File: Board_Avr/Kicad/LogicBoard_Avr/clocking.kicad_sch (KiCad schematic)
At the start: 5 parts, among them X1 ASV-12.000MHZ-EJ-T, Y1 ABLS-20.000MHz-16-A-4-H-T

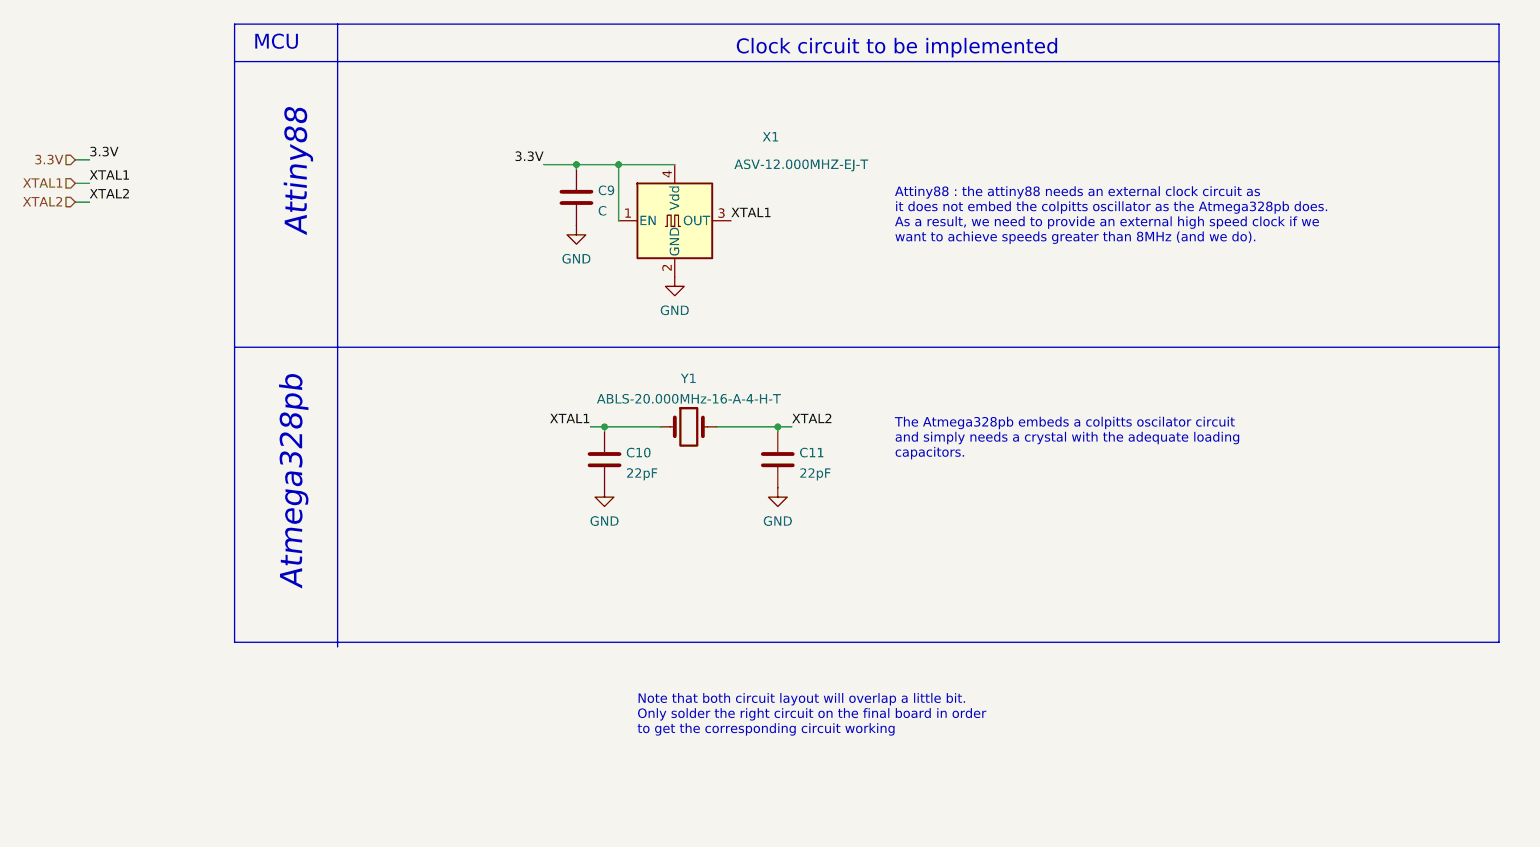
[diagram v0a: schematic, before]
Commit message: Added several external connections and reworked leds and output signals
Signed-off-by: bebenlebricolo <benoittarrade@hotmail.fr>
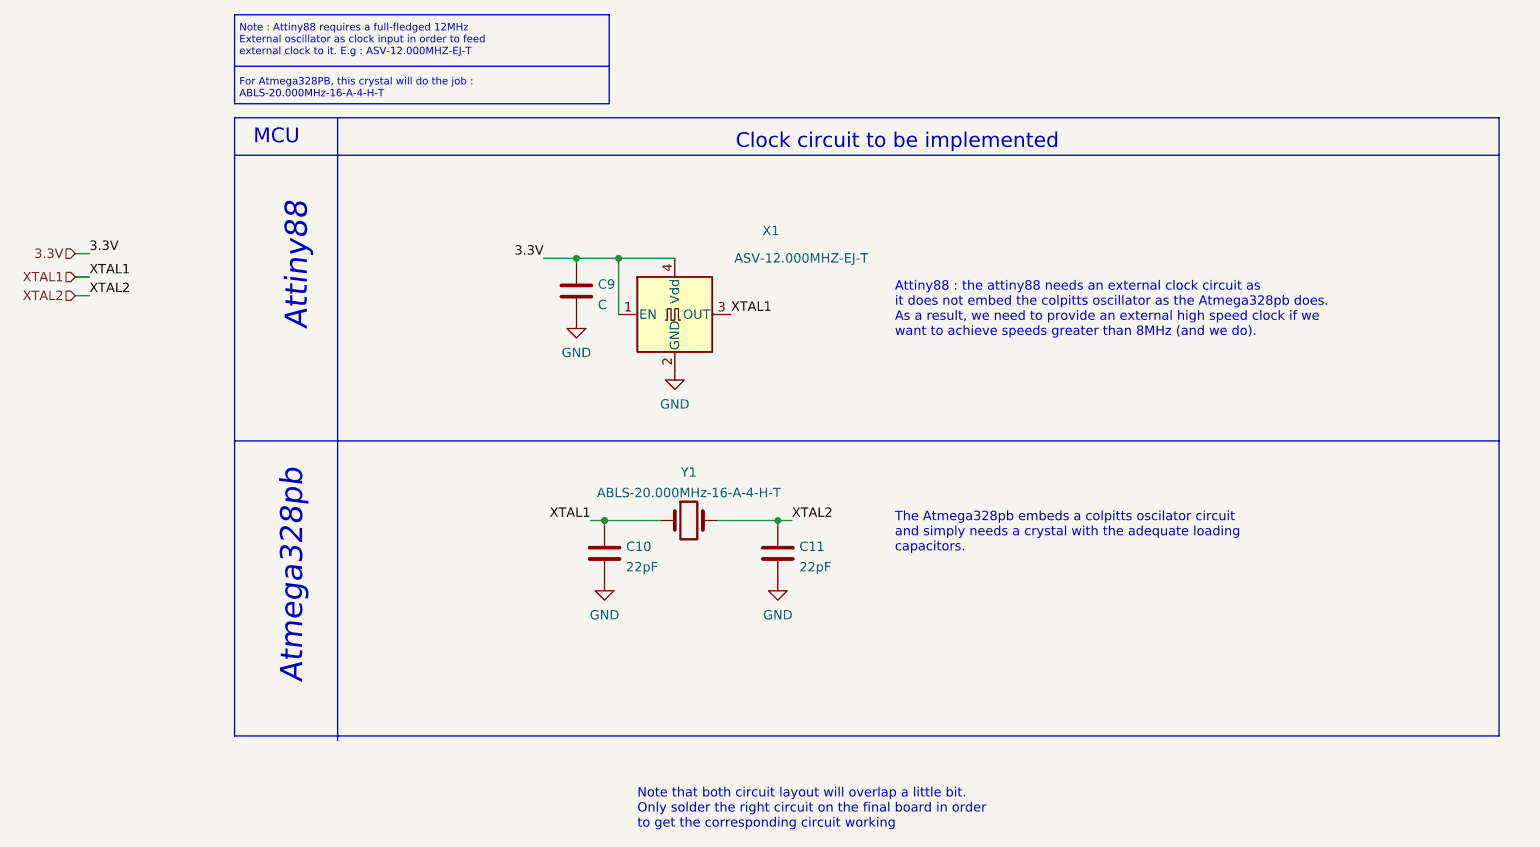
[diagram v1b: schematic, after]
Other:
- note added: "For Atmega328PB, this crystal will do the job : ABLS-20.000MHz-16-A-4-H-T"
- note added: "Note : Attiny88 requires a full-fledged 12MHz External oscillator as clock input in order to feed external clock to it. E.g : ASV-12.000MHZ-EJ-T"
- moved on the sheet: C10, C11, C9, X1, Y1

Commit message: Started routing all traces
Signed-off-by: bebenlebricolo <benoittarrade@hotmail.fr>
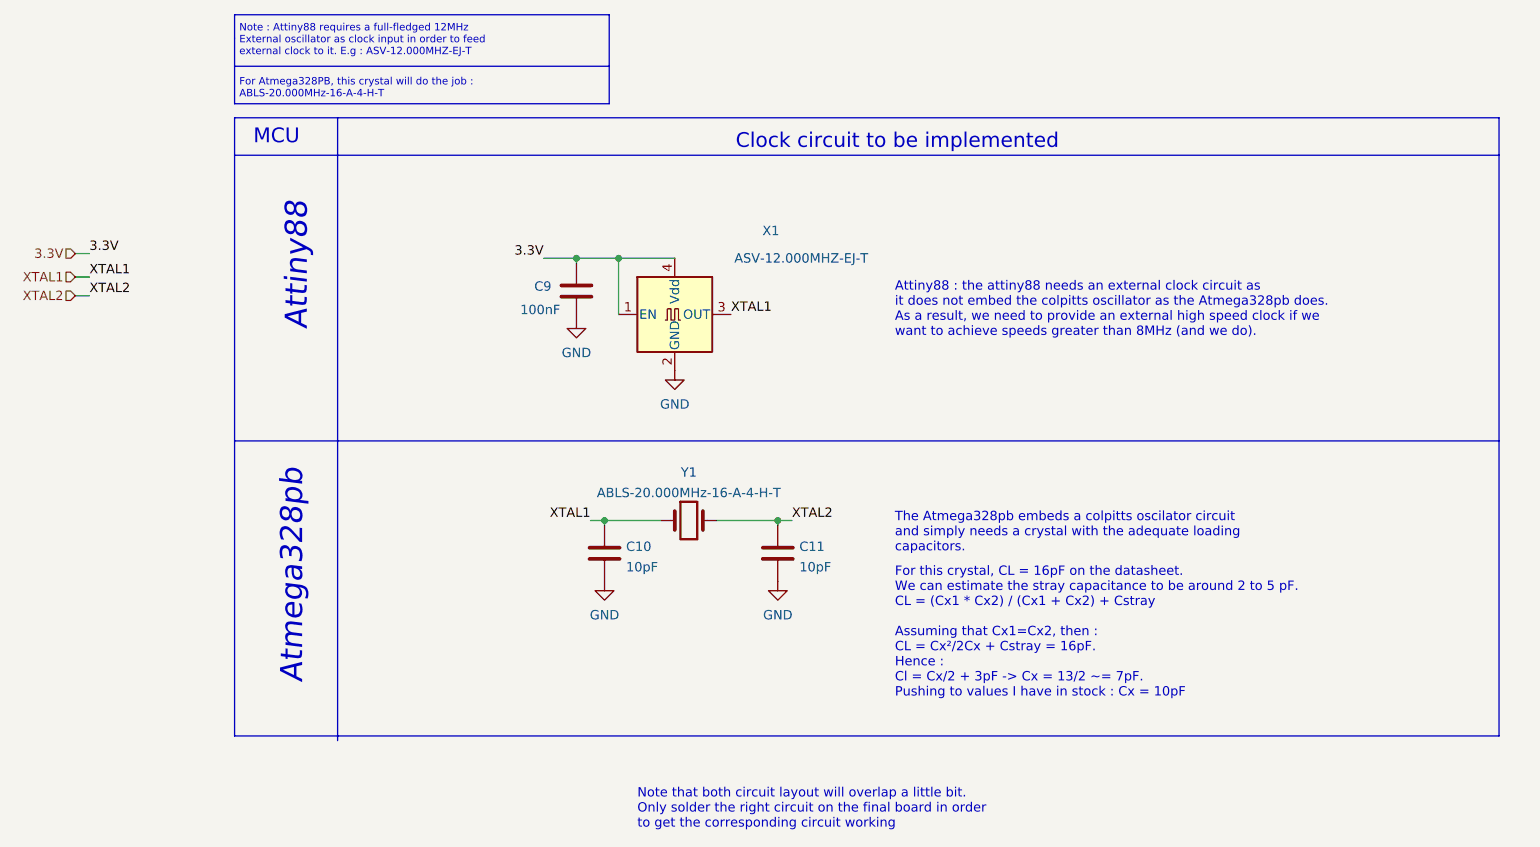
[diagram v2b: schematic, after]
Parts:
- C10, C11: value 22pF -> 10pF; footprint (none) -> Capacitor_SMD:C_1206_3216Metric
- C9: value C -> 100nF; footprint (none) -> Capacitor_SMD:C_1206_3216Metric
- Y1: footprint (none) -> Crystal:Crystal_SMD_HC49-SD
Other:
- note added: "For this crystal, CL = 16pF on the datasheet. We can estimate the stray capacitance to be around 2 to 5 pF. CL = (Cx1 * Cx2) / (Cx1 + Cx2) + Cstray Assuming that Cx1=Cx2, then : CL = Cx²/2Cx + Cstray = 16pF. Hence : Cl = Cx/2 + 3pF -> Cx = 13/2 ~= 7pF. Pushing to values I have in stock : Cx = 10pF"
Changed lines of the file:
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@@
+    (effects (font (size 1.27 1.27)) (justify left bottom))
+  )
+  (text "For this crystal, CL = 16pF on the datasheet.\nWe can estimate the stray capacitance to be around 2 to 5 pF.\nCL = (Cx1 * Cx2) / (Cx1 + Cx2) + Cstray\n\nAssuming that Cx1=Cx2, then : \nCL = Cx²/2Cx + Cstray = 16pF.\nHence :\nCl = Cx/2 + 3pF -> Cx = 13/2 ~= 7pF.\nPushing to values I have in stock : Cx = 10pF"
+    (at 165.1 125.095 0)
     (effects (font (size 1.27 1.27)) (justify left bottom))
   )
@@
   )
   (symbol (lib_id "Device:C") (at 121.92 69.85 0) (unit 1)
-    (in_bom yes) (on_board yes) (fields_autoplaced)
-    (property "Reference" "C9" (id 0) (at 124.841 68.9415 0)
+    (in_bom yes) (on_board yes)
+    (property "Reference" "C9" (id 0) (at 116.205 69.215 0)
       (effects (font (size 1.27 1.27)) (justify left))
     )
-    (property "Value" "C" (id 1) (at 124.841 71.7166 0)
+    (property "Value" "100nF" (id 1) (at 114.3 72.39 0)
       (effects (font (size 1.27 1.27)) (justify left))
     )
-    (property "Footprint" "" (id 2) (at 122.8852 73.66 0)
+    (property "Footprint" "Capacitor_SMD:C_1206_3216Metric" (id 2) (at 122.8852 73.66 0)
       (effects (font (size 1.27 1.27)) hide)
     )
@@
       (effects (font (size 1.27 1.27)) (justify left))
     )
-    (property "Value" "22pF" (id 1) (at 128.651 107.2766 0)
+    (property "Value" "10pF" (id 1) (at 128.651 107.2766 0)
       (effects (font (size 1.27 1.27)) (justify left))
     )
-    (property "Footprint" "" (id 2) (at 126.6952 109.22 0)
+    (property "Footprint" "Capacitor_SMD:C_1206_3216Metric" (id 2) (at 126.6952 109.22 0)
       (effects (font (size 1.27 1.27)) hide)
     )
@@
     (property "Reference" "Y1" (id 0) (at 137.16 94.4331 0))
     (property "Value" "ABLS-20.000MHz-16-A-4-H-T" (id 1) (at 137.16 97.2082 0))
-    (property "Footprint" "" (id 2) (at 137.16 100.965 0)
+    (property "Footprint" "Crystal:Crystal_SMD_HC49-SD" (id 2) (at 137.16 100.965 0)
       (effects (font (size 1.27 1.27)) hide)
     )
@@
       (effects (font (size 1.27 1.27)) (justify left))
     )
-    (property "Value" "22pF" (id 1) (at 152.146 107.2766 0)
+    (property "Value" "10pF" (id 1) (at 152.146 107.2766 0)
       (effects (font (size 1.27 1.27)) (justify left))
     )
-    (property "Footprint" "" (id 2) (at 150.1902 109.22 0)
+    (property "Footprint" "Capacitor_SMD:C_1206_3216Metric" (id 2) (at 150.1902 109.22 0)
       (effects (font (size 1.27 1.27)) hide)
     )

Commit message: Replaced TLV1117-3.3 by NCP630SN330 and polished a bit zoning
Signed-off-by: bebenlebricolo <benoittarrade@hotmail.fr>
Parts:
- Y1: footprint Crystal:Crystal_SMD_HC49-SD -> BTS-LogicBoard:Crystal_SMD_TH_Combo_HC49-SD
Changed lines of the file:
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@@
     (property "Reference" "Y1" (id 0) (at 137.16 94.4331 0))
     (property "Value" "ABLS-20.000MHz-16-A-4-H-T" (id 1) (at 137.16 97.2082 0))
-    (property "Footprint" "Crystal:Crystal_SMD_HC49-SD" (id 2) (at 137.16 100.965 0)
+    (property "Footprint" "BTS-LogicBoard:Crystal_SMD_TH_Combo_HC49-SD" (id 2) (at 137.16 100.965 0)
       (effects (font (size 1.27 1.27)) hide)
     )

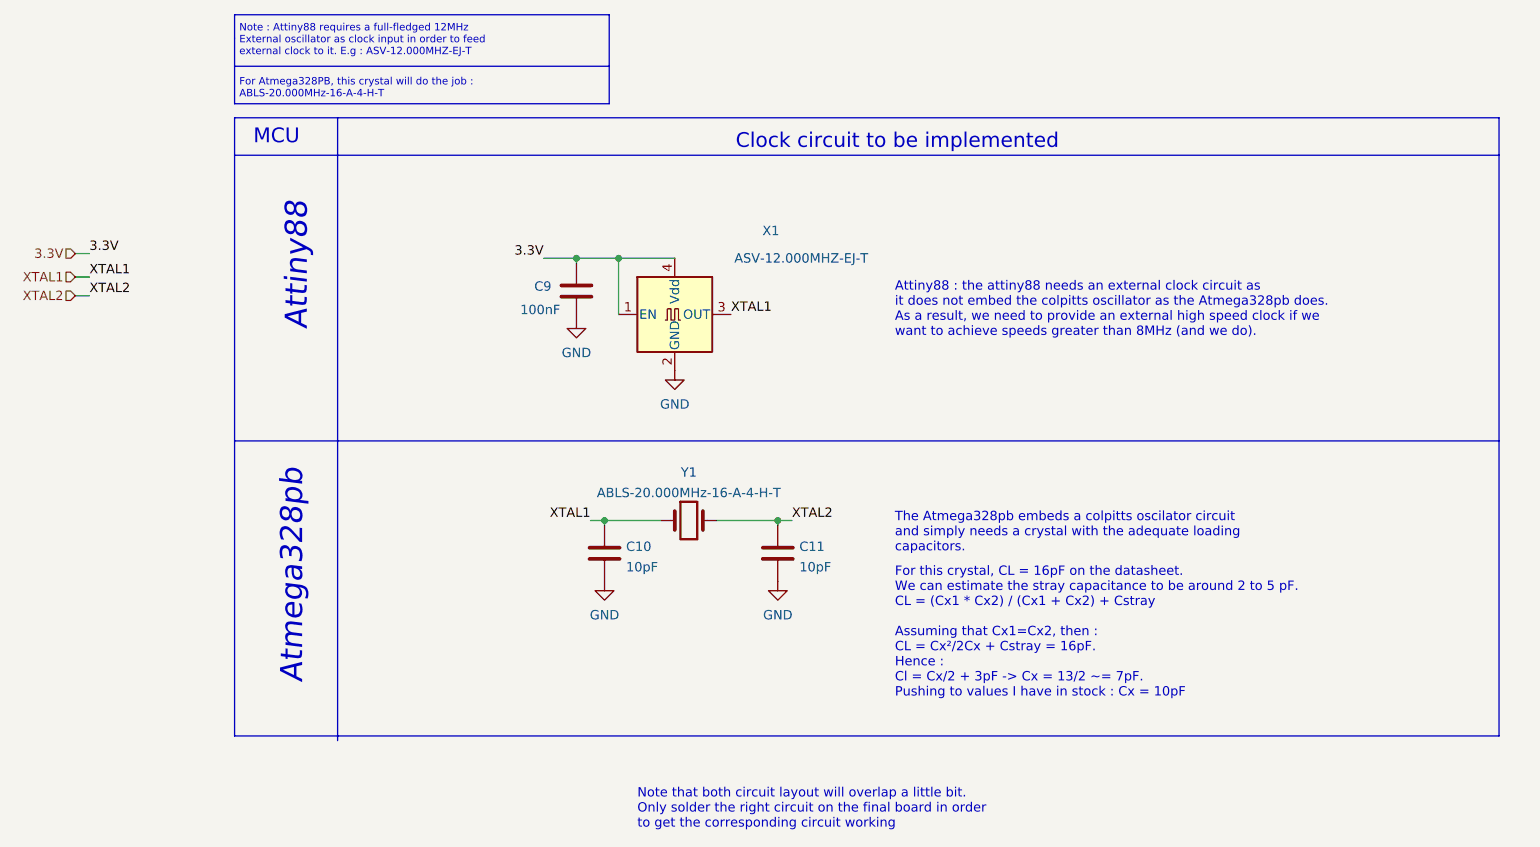
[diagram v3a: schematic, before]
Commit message: Updated board with external clock for both mcus + thermal reliefs update
Signed-off-by: bebenlebricolo <benoittarrade@hotmail.fr>
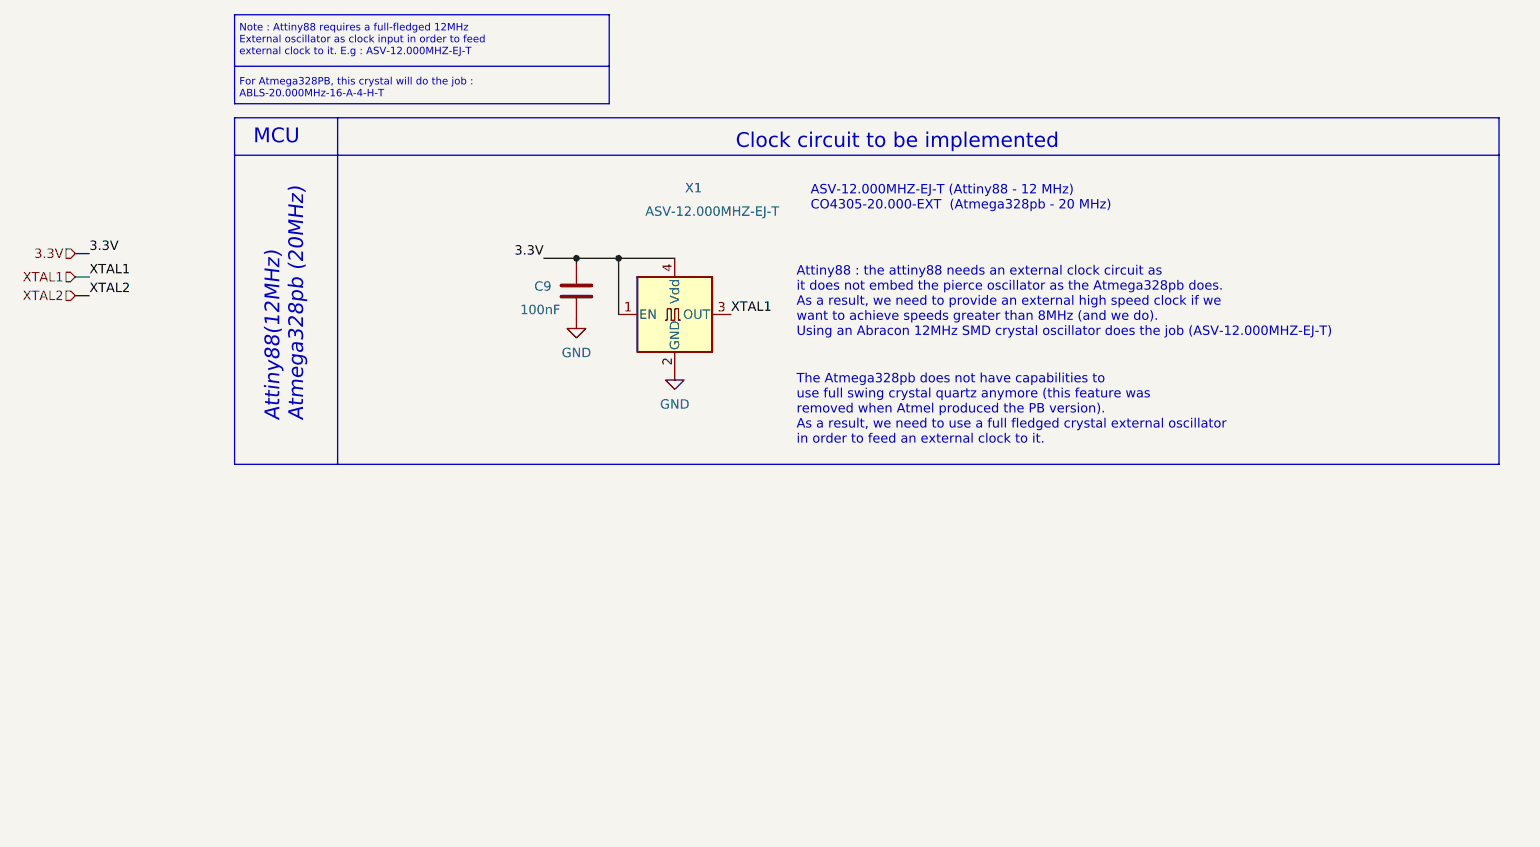
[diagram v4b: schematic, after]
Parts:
- removed C10, C11: 10pF, Capacitor_SMD:C_1206_3216Metric, symbol Device:C
- removed Y1: ABLS-20.000MHz-16-A-4-H-T, BTS-LogicBoard:Crystal_SMD_TH_Combo_HC49-SD, symbol Device:Crystal
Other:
- note added: "ASV-12.000MHZ-EJ-T (Attiny88 - 12 MHz) CO4305-20.000-EXT (Atmega328pb - 20 MHz)"
- note added: "Attiny88 : the attiny88 needs an external clock circuit as it does not embed the pierce oscillator as the Atmega328pb does. As a result, we need to provide an external high speed clock if we want to achieve speeds greater than 8MHz (and we do). Using an Abracon 12MHz SMD crystal oscillator does the job (ASV-12.000MHZ-EJ-T)"
- note added: "Attiny88(12MHz) Atmega328pb (20MHz)"
- note added: "The Atmega328pb does not have capabilities to use full swing crystal quartz anymore (this feature was removed when Atmel produced the PB version). As a result, we need to use a full fledged crystal external oscillator in order to feed an external clock to it."
- note removed: "Atmega328pb"
- note removed: "Attiny88"
- note removed: "Attiny88 : the attiny88 needs an external clock circuit as it does not embed the colpitts oscillator as the Atmega328pb does. As a result, we need to provide an external high speed clock if we want to achieve speeds greater than 8MHz (and we do)."
- note removed: "For this crystal, CL = 16pF on the datasheet. We can estimate the stray capacitance to be around 2 to 5 pF. CL = (Cx1 * Cx2) / (Cx1 + Cx2) + Cstray Assuming that Cx1=Cx2, then : CL = Cx²/2Cx + Cstray = 16pF. Hence : Cl = Cx/2 + 3pF -> Cx = 13/2 ~= 7pF. Pushing to values I have in stock : Cx = 10pF"
- note removed: "Note that both circuit layout will overlap a little bit. Only solder the right circuit on the final board in order to get the corresponding circuit working"
- note removed: "The Atmega328pb embeds a colpitts oscilator circuit and simply needs a crystal with the adequate loading capacitors."
